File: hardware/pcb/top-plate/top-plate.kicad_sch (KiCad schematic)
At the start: 4 parts

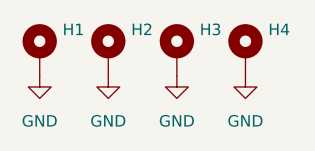
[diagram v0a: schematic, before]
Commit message: update documentation images, remove copper pours and vias from top plate, minor fixes
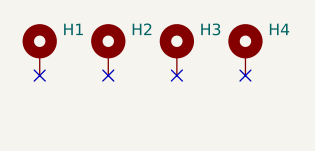
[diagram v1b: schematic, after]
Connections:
- removed net GND: H1.1, H2.1, H3.1, H4.1
- no-connect marks 0 -> 4

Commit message: changed m2.5 mh to m2, added screws and nuts to enclosure.FCStd
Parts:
- H1, H2, H3, H4: footprint MountingHole:MountingHole_2.5mm_Pad -> MountingHole:MountingHole_2.2mm_M2_DIN965_Pad
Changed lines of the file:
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@@
 			)
 		)
-		(property "Footprint" "MountingHole:MountingHole_2.5mm_Pad"
+		(property "Footprint" "MountingHole:MountingHole_2.2mm_M2_DIN965_Pad"
 			(at 154.94 101.6 0)
 			(effects
@@
 			)
 		)
-		(property "Footprint" "MountingHole:MountingHole_2.5mm_Pad"
+		(property "Footprint" "MountingHole:MountingHole_2.2mm_M2_DIN965_Pad"
 			(at 147.32 101.6 0)
 			(effects
@@
 			)
 		)
-		(property "Footprint" "MountingHole:MountingHole_2.5mm_Pad"
+		(property "Footprint" "MountingHole:MountingHole_2.2mm_M2_DIN965_Pad"
 			(at 139.7 101.6 0)
 			(effects
@@
 			)
 		)
-		(property "Footprint" "MountingHole:MountingHole_2.5mm_Pad"
+		(property "Footprint" "MountingHole:MountingHole_2.2mm_M2_DIN965_Pad"
 			(at 132.08 101.6 0)
 			(effects
